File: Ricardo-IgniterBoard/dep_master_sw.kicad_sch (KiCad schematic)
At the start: 12 parts, among them Q5 BSZ025N04LS, Q6 BSZ025N04LS, U8 LM74810

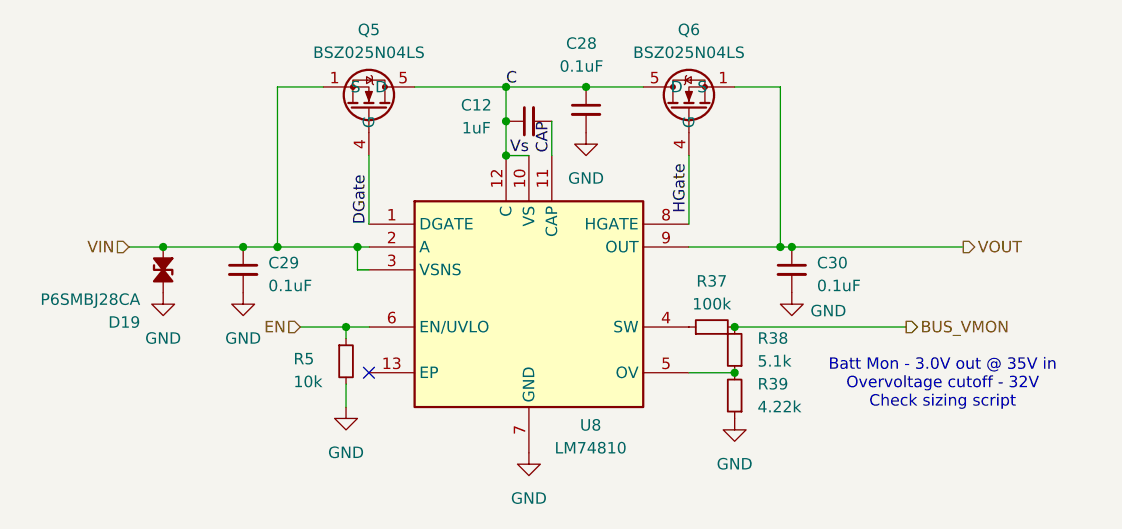
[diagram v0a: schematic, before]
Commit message: Assigning components
And added the thermocouple
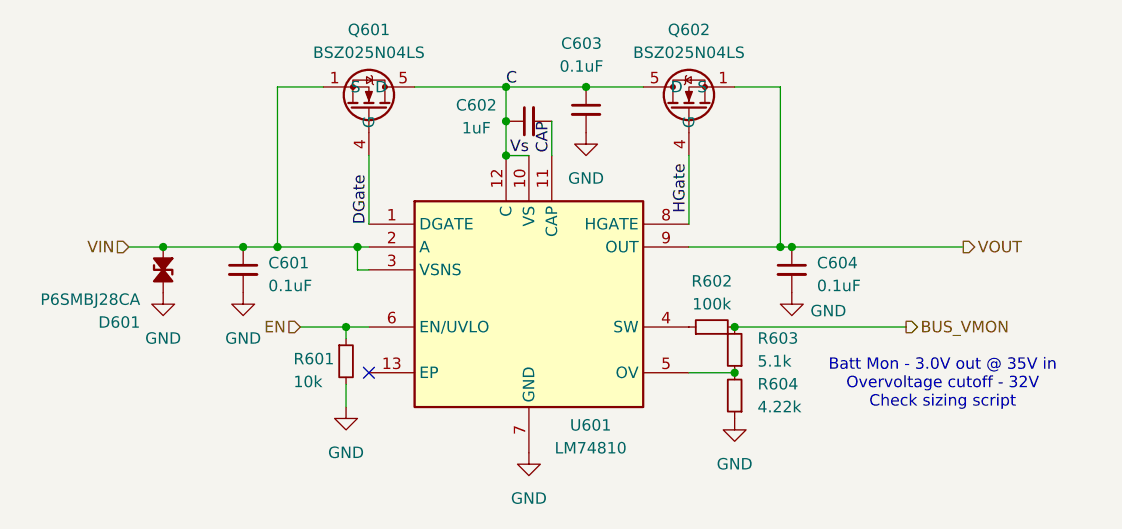
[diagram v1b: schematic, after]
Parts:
- renumbered C29 to C601, C12 to C602, C28 to C603, C30 to C604, D19 to D601, Q5 to Q601, Q6 to Q602, R5 to R601, R37 to R602, R38 to R603, R39 to R604, U8 to U601
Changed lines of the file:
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@@
 		(on_board yes)
 		(dnp no)
-		(property "Reference" "C29"
+		(property "Reference" "C601"
 			(at 110.744 64.008 0)
 			(effects
@@
 			(project ""
 				(path "/7db990e4-92e1-4f99-b4d2-435bbec1ba83/6eddec06-ec63-40e5-b1db-333261e0d1b4"
-					(reference "C29")
+					(reference "C601")
 					(unit 1)
 				)
@@
 		(on_board yes)
 		(dnp no)
-		(property "Reference" "C12"
+		(property "Reference" "C602"
 			(at 133.858 46.482 90)
 			(effects
@@
 			(project ""
 				(path "/7db990e4-92e1-4f99-b4d2-435bbec1ba83/6eddec06-ec63-40e5-b1db-333261e0d1b4"
-					(reference "C12")
+					(reference "C602")
 					(unit 1)
 				)
@@
 		(on_board yes)
 		(dnp no)
-		(property "Reference" "C28"
+		(property "Reference" "C603"
 			(at 145.542 39.624 0)
 			(effects
@@
 			(project "flintandsteel"
 				(path "/7db990e4-92e1-4f99-b4d2-435bbec1ba83/6eddec06-ec63-40e5-b1db-333261e0d1b4"
-					(reference "C28")
+					(reference "C603")
 					(unit 1)
 				)
@@
 		(dnp no)
 		(fields_autoplaced yes)
-		(property "Reference" "Q6"
+		(property "Reference" "Q602"
 			(at 157.48 38.1 90)
 			(effects
@@
 			(project ""
 				(path "/7db990e4-92e1-4f99-b4d2-435bbec1ba83/6eddec06-ec63-40e5-b1db-333261e0d1b4"
-					(reference "Q6")
+					(reference "Q602")
 					(unit 1)
 				)
@@
 		(dnp no)
 		(fields_autoplaced yes)
-		(property "Reference" "R37"
+		(property "Reference" "R602"
 			(at 160.02 66.04 90)
 			(effects
@@
 			(project ""
 				(path "/7db990e4-92e1-4f99-b4d2-435bbec1ba83/6eddec06-ec63-40e5-b1db-333261e0d1b4"
-					(reference "R37")
+					(reference "R602")
 					(unit 1)
 				)
@@
 		(on_board yes)
 		(dnp no)
-		(property "Reference" "C30"
+		(property "Reference" "C604"
 			(at 171.704 64.008 0)
 			(effects
@@
 			(project "flintandsteel"
 				(path "/7db990e4-92e1-4f99-b4d2-435bbec1ba83/6eddec06-ec63-40e5-b1db-333261e0d1b4"
-					(reference "C30")
+					(reference "C604")
 					(unit 1)
 				)
@@
 		(dnp no)
 		(fields_autoplaced yes)
-		(property "Reference" "R38"
+		(property "Reference" "R603"
 			(at 165.1 72.3899 0)
 			(effects
@@
 			(project "flintandsteel"
 				(path "/7db990e4-92e1-4f99-b4d2-435bbec1ba83/6eddec06-ec63-40e5-b1db-333261e0d1b4"
-					(reference "R38")
+					(reference "R603")
 					(unit 1)
 				)
@@
 		(dnp no)
 		(fields_autoplaced yes)
-		(property "Reference" "#PWR015"
+		(property "Reference" "#PWR0112"
 			(at 119.38 86.36 0)
 			(effects
@@
 			(project ""
 				(path "/7db990e4-92e1-4f99-b4d2-435bbec1ba83/6eddec06-ec63-40e5-b1db-333261e0d1b4"
-					(reference "#PWR015")
+					(reference "#PWR0112")
 					(unit 1)
 				)
@@
 		(on_board yes)
 		(dnp no)
-		(property "Reference" "U8"
+		(property "Reference" "U601"
 			(at 146.558 82.042 0)
 			(effects
@@
 			(project ""
 				(path "/7db990e4-92e1-4f99-b4d2-435bbec1ba83/6eddec06-ec63-40e5-b1db-333261e0d1b4"
-					(reference "U8")
+					(reference "U601")
 					(unit 1)
 				)
@@
 		(dnp no)
 		(fields_autoplaced yes)
-		(property "Reference" "R39"
+		(property "Reference" "R604"
 			(at 165.1 77.4699 0)
 			(effects
@@
 			(project "flintandsteel"
 				(path "/7db990e4-92e1-4f99-b4d2-435bbec1ba83/6eddec06-ec63-40e5-b1db-333261e0d1b4"
-					(reference "R39")
+					(reference "R604")
 					(unit 1)
 				)
@@
 		(on_board yes)
 		(dnp no)
-		(property "Reference" "R5"
+		(property "Reference" "R601"
 			(at 113.538 74.676 0)
 			(effects
@@
 			(project ""
 				(path "/7db990e4-92e1-4f99-b4d2-435bbec1ba83/6eddec06-ec63-40e5-b1db-333261e0d1b4"
-					(reference "R5")
+					(reference "R601")
 					(unit 1)
 				)
@@
 		(on_board yes)
 		(dnp no)
-		(property "Reference" "Q5"
+		(property "Reference" "Q601"
 			(at 121.92 38.1 90)
 			(effects
@@
 			(project "flintandsteel"
 				(path "/7db990e4-92e1-4f99-b4d2-435bbec1ba83/6eddec06-ec63-40e5-b1db-333261e0d1b4"
-					(reference "Q5")
+					(reference "Q601")
 					(unit 1)
 				)
@@
 		(dnp no)
 		(fields_autoplaced yes)
-		(property "Reference" "#PWR09"
+		(property "Reference" "#PWR0108"
 			(at 139.7 91.44 0)
 			(effects
@@
 			(project "flintandsteel"
 				(path "/7db990e4-92e1-4f99-b4d2-435bbec1ba83/6eddec06-ec63-40e5-b1db-333261e0d1b4"
-					(reference "#PWR09")
+					(reference "#PWR0108")
 					(unit 1)
 				)
@@
 		(on_board yes)
 		(dnp no)
-		(property "Reference" "D19"
+		(property "Reference" "D601"
 			(at 96.52 70.612 90)
 			(effects
@@
 			(project ""
 				(path "/7db990e4-92e1-4f99-b4d2-435bbec1ba83/6eddec06-ec63-40e5-b1db-333261e0d1b4"
-					(reference "D19")
-					(unit 1)
-				)
+					(reference "D601")
+					(unit 1)
+				)
